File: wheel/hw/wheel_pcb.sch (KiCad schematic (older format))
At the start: 43 parts, among them J2 DEBUG, J3 IO_C, J4 CAR, J5 IO_B, J6 IO_A, SW1 CONFIG, U1 LPC11C24FBD48, U2 TPS62175, U3 TLV70233_SOT23-5, U4 SP4065-08ATG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

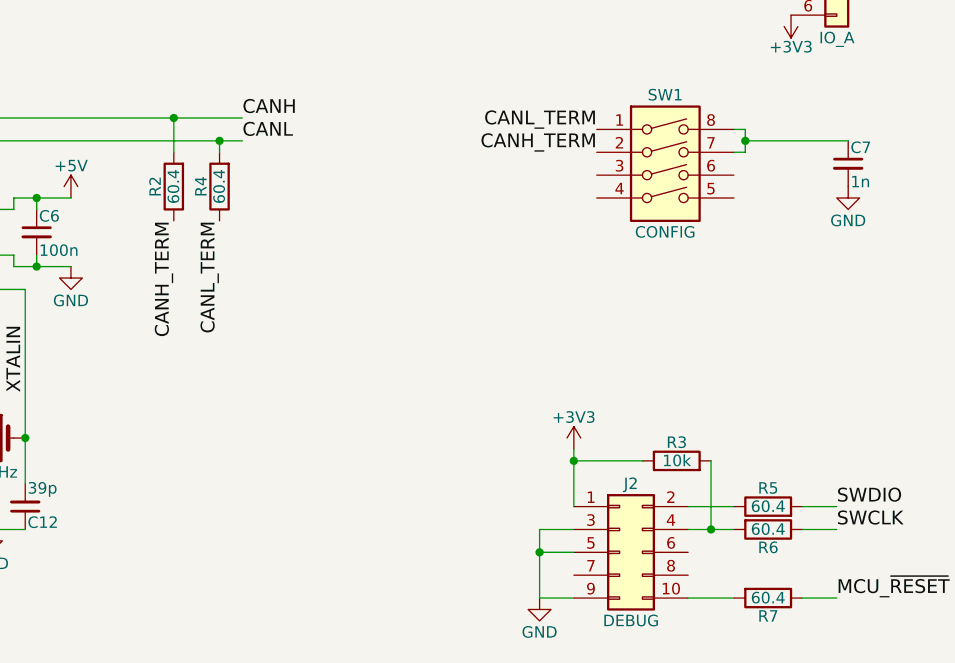
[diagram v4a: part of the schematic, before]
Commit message: sensibilize resistor values
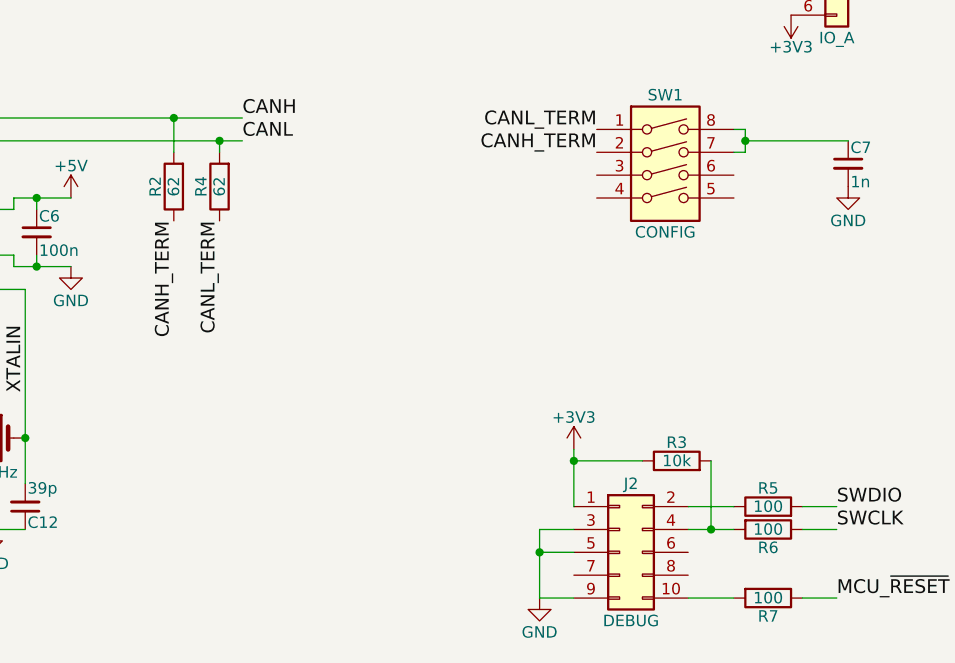
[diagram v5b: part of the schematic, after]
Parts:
- R2, R4: value 60.4 -> 62
- R5, R6: value 60.4 -> 100
- R7: value 60.4 -> 100; footprint Resistors_SMD:R_0603 -> (none)
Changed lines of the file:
@@
 P 7750 4500
 F 0 "R2" V 7830 4500 50  0000 C CNN
-F 1 "60.4" V 7750 4500 50  0000 C CNN
+F 1 "62" V 7750 4500 50  0000 C CNN
 F 2 "Resistors_SMD:R_0603" V 7680 4500 50  0001 C CNN
-F 3 "https://www.mouser.de/ProductDetail/Bourns/CR0603-FX-60R4ELF?qs=sGAEpiMZZMu61qfTUdNhG6LqqFhkr6pUa8gjAX4b5rM%3d" H 7750 4500 50  0001 C CNN
+F 3 "https://www.mouser.de/ProductDetail/Bourns/CR0603-FX-62R0ELF?qs=0nF2VnfAjXnEYbikTYe9aw%3d%3d" H 7750 4500 50  0001 C CNN
 	1    7750 4500
 	-1   0    0    1
@@
 P 7950 4500
 F 0 "R4" V 8030 4500 50  0000 C CNN
-F 1 "60.4" V 7950 4500 50  0000 C CNN
+F 1 "62" V 7950 4500 50  0000 C CNN
 F 2 "Resistors_SMD:R_0603" V 7880 4500 50  0001 C CNN
-F 3 "https://www.mouser.de/ProductDetail/Bourns/CR0603-FX-60R4ELF?qs=sGAEpiMZZMu61qfTUdNhG6LqqFhkr6pUa8gjAX4b5rM%3d" H 7950 4500 50  0001 C CNN
+F 3 "https://www.mouser.de/ProductDetail/Bourns/CR0603-FX-62R0ELF?qs=0nF2VnfAjXnEYbikTYe9aw%3d%3d" H 7950 4500 50  0001 C CNN
 	1    7950 4500
 	-1   0    0    1
@@
 P 10350 5900
 F 0 "R5" V 10430 5900 50  0000 C CNN
-F 1 "60.4" V 10350 5900 50  0000 C CNN
+F 1 "100" V 10350 5900 50  0000 C CNN
 F 2 "Resistors_SMD:R_0603" V 10280 5900 50  0001 C CNN
-F 3 "https://www.mouser.de/ProductDetail/Bourns/CR0603-FX-60R4ELF?qs=sGAEpiMZZMu61qfTUdNhG6LqqFhkr6pUa8gjAX4b5rM%3d" H 10350 5900 50  0001 C CNN
+F 3 "" H 10350 5900 50  0001 C CNN
 	1    10350 5900
 	0    -1   -1   0
@@
 P 10350 6000
 F 0 "R6" V 10430 6000 50  0000 C CNN
-F 1 "60.4" V 10350 6000 50  0000 C CNN
+F 1 "100" V 10350 6000 50  0000 C CNN
 F 2 "Resistors_SMD:R_0603" V 10280 6000 50  0001 C CNN
-F 3 "https://www.mouser.de/ProductDetail/Bourns/CR0603-FX-60R4ELF?qs=sGAEpiMZZMu61qfTUdNhG6LqqFhkr6pUa8gjAX4b5rM%3d" H 10350 6000 50  0001 C CNN
+F 3 "" H 10350 6000 50  0001 C CNN
 	1    10350 6000
 	0    1    1    0
@@
 P 10350 6300
 F 0 "R7" V 10430 6300 50  0000 C CNN
-F 1 "60.4" V 10350 6300 50  0000 C CNN
-F 2 "Resistors_SMD:R_0603" V 10280 6300 50  0001 C CNN
+F 1 "100" V 10350 6300 50  0000 C CNN
+F 2 "" V 10280 6300 50  0001 C CNN
 F 3 "https://www.mouser.de/ProductDetail/Bourns/CR0603-FX-60R4ELF?qs=sGAEpiMZZMu61qfTUdNhG6LqqFhkr6pUa8gjAX4b5rM%3d" H 10350 6300 50  0001 C CNN
 	1    10350 6300

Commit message: make 2 position slide switches instead of 4
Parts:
- R7: footprint (none) -> Resistors_SMD:R_0603
- SW1: value CONFIG -> TERM; footprint Buttons_Switches_THT:SW_DIP_x4_W7.62mm_Slide -> Buttons_Switches_THT:SW_DIP_x2_W7.62mm_Slide; symbol SW_DIP_x04 -> SW_DIP_x02
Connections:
- net at SW1.3: now also C7.1, SW1.4
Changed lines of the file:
@@
 F 0 "R7" V 10430 6300 50  0000 C CNN
 F 1 "100" V 10350 6300 50  0000 C CNN
-F 2 "" V 10280 6300 50  0001 C CNN
+F 2 "Resistors_SMD:R_0603" V 10280 6300 50  0001 C CNN
 F 3 "https://www.mouser.de/ProductDetail/Bourns/CR0603-FX-60R4ELF?qs=sGAEpiMZZMu61qfTUdNhG6LqqFhkr6pUa8gjAX4b5rM%3d" H 10350 6300 50  0001 C CNN
 	1    10350 6300
@@
 $EndComp
 $Comp
-L SW_DIP_x04 SW1
+L SW_DIP_x02 SW1
 U 1 1 5AFC4E3D
-P 9900 4450
-F 0 "SW1" H 9900 4800 50  0000 C CNN
-F 1 "CONFIG" H 9900 4200 50  0000 C CNN
-F 2 "Buttons_Switches_THT:SW_DIP_x4_W7.62mm_Slide" H 9900 4450 50  0001 C CNN
-F 3 "https://www.mouser.de/ProductDetail/TE-Connectivity-Alcoswitch/ADE0404?qs=sGAEpiMZZMv%2f%252b2JhlA6ysER62VlXw6iZ4HTlb4kKXdw%3d" H 9900 4450 50  0001 C CNN
-	1    9900 4450
-	1    0    0    -1
-$EndComp
+P 9900 4350
+F 0 "SW1" H 9900 4600 50  0000 C CNN
+F 1 "TERM" H 9900 4200 50  0000 C CNN
+F 2 "Buttons_Switches_THT:SW_DIP_x2_W7.62mm_Slide" H 9900 4350 50  0001 C CNN
+F 3 "https://www.mouser.de/ProductDetail/Apem/NDS02V?qs=sGAEpiMZZMvHnN%252b%2fGH9WnarhEfYmPrhIFZ2OxET8b5I%3d" H 9900 4350 50  0001 C CNN
+	1    9900 4350
+	1    0    0    -1
+$EndComp

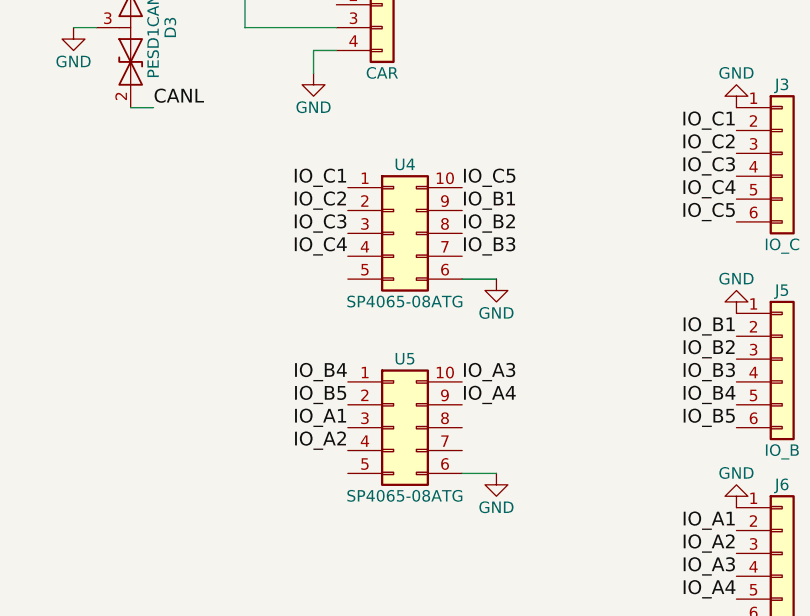
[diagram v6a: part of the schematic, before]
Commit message: draft layout of new wheel stuff
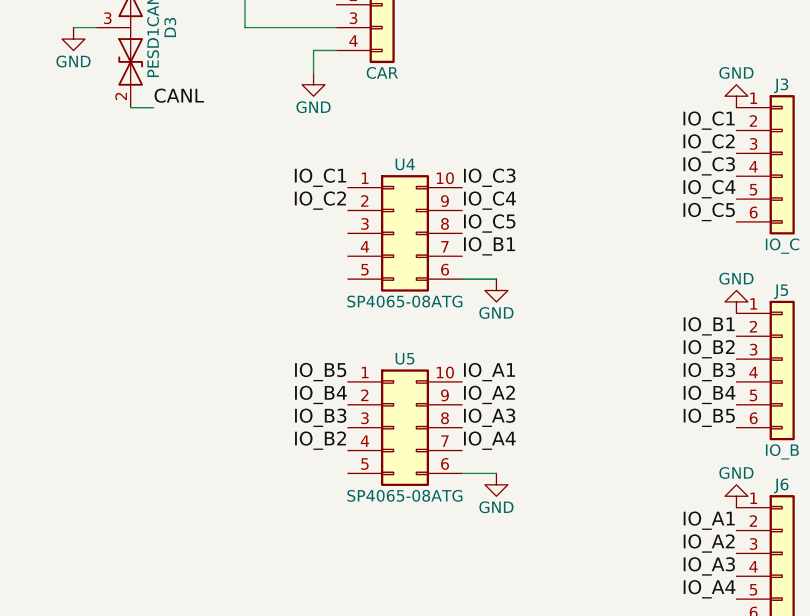
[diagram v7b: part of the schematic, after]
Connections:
- net IO_A1: now also U5.10 (Pin_10); no longer U5.3 (Pin_3)
- net IO_A2: now also U5.9 (Pin_9); no longer U5.4 (Pin_4)
- net IO_A3: now also U5.8 (Pin_8); no longer U5.10 (Pin_10)
- net IO_A4: now also U5.7 (Pin_7); no longer U5.9 (Pin_9)
- net IO_B1: now also U4.7 (Pin_7); no longer U4.9 (Pin_9)
- net IO_B2: now also U5.4 (Pin_4); no longer U4.8 (Pin_8)
- net IO_B3: now also U5.3 (Pin_3); no longer U4.7 (Pin_7)
- net IO_B4: now also U5.2 (Pin_2); no longer U5.1 (Pin_1)
- net IO_B5: now also U5.1 (Pin_1); no longer U5.2 (Pin_2)
- net IO_C3: now also U4.10 (Pin_10); no longer U4.3 (Pin_3)
- net IO_C4: now also U4.9 (Pin_9); no longer U4.4 (Pin_4)
- net IO_C5: now also U4.8 (Pin_8); no longer U4.10 (Pin_10)
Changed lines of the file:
@@
 Wire Wire Line
 	7550 1150 7650 1150
-Text Label 8750 3000 2    60   ~ 0
-IO_A2
-Text Label 8750 2900 2    60   ~ 0
-IO_A1
-Text Label 8750 2800 2    60   ~ 0
-IO_B5
-Text Label 8750 2700 2    60   ~ 0
-IO_B4
 Wire Wire Line
 	9250 3100 9400 3100
@@
 	1    0    0    -1
 $EndComp
-Text Label 9250 2150 0    60   ~ 0
-IO_B3
-Text Label 9250 2050 0    60   ~ 0
-IO_B2
-Text Label 9250 1950 0    60   ~ 0
-IO_B1
-Text Label 9250 1850 0    60   ~ 0
-IO_C5
-Text Label 8750 2150 2    60   ~ 0
-IO_C4
-Text Label 8750 2050 2    60   ~ 0
-IO_C3
-Text Label 8750 1950 2    60   ~ 0
-IO_C2
-Text Label 8750 1850 2    60   ~ 0
-IO_C1
 Wire Wire Line
 	9250 2250 9400 2250
@@
 	1    0    0    -1
 $EndComp
-Text Label 9250 2700 0    60   ~ 0
-IO_A3
-Text Label 9250 2800 0    60   ~ 0
-IO_A4
 Wire Wire Line
 	7800 800  7900 800
+Text Label 8750 1850 2    60   ~ 0
+IO_C1
+Text Label 8750 1950 2    60   ~ 0
+IO_C2
+Text Label 9250 1850 0    60   ~ 0
+IO_C3
+Text Label 9250 1950 0    60   ~ 0
+IO_C4
+Text Label 9250 2050 0    60   ~ 0
+IO_C5
+Text Label 9250 2150 0    60   ~ 0
+IO_B1
+Text Label 8750 2700 2    60   ~ 0
+IO_B5
+Text Label 8750 2800 2    60   ~ 0
+IO_B4
+Text Label 8750 2900 2    60   ~ 0
+IO_B3
+Text Label 8750 3000 2    60   ~ 0
+IO_B2
+Text Label 9250 2700 0    60   ~ 0
+IO_A1
+Text Label 9250 2800 0    60   ~ 0
+IO_A2
+Text Label 9250 2900 0    60   ~ 0
+IO_A3
+Text Label 9250 3000 0    60   ~ 0
+IO_A4
 $EndSCHEMATC

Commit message: add alternate part number for programming connector
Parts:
- J2: Datasheet2 (none) -> de.farnell.com/samtec/shf-105-01-l-d-ra/stiftleiste-10-pos-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
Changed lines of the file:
@@
 F 2 "custom_footprints:Pin_Header_Angled_2x05_Pitch1.27mm_AMPHENOL_SHROUDED" H 9700 6100 50  0001 C CNN
 F 3 "https://www.mouser.de/ProductDetail/Amphenol-FCI/20021512-00010T4LF?qs=sGAEpiMZZMs%252bGHln7q6pmwodwKqstCemugheqdGIyCk%3d" H 9700 6100 50  0001 C CNN
+F 4 "de.farnell.com/samtec/shf-105-01-l-d-ra/stiftleiste-10-pos-2-reihen-1/dp/2505002?st=SHF-105-01-L-D-RA" H 9700 6100 60  0001 C CNN "Datasheet2"
 	1    9700 6100
 	1    0    0    -1
